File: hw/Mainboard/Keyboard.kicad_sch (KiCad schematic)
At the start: 5 parts, among them J2 KEYBOARD, U1 74LS145

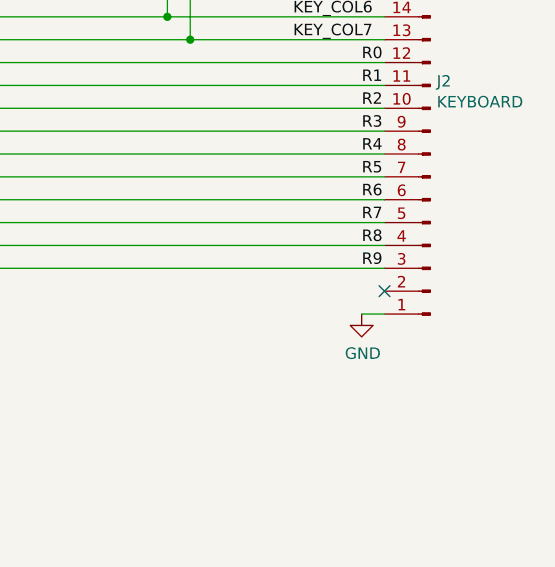
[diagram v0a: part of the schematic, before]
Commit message: hw: routed, but trace sizes need to be reviewed/fixed
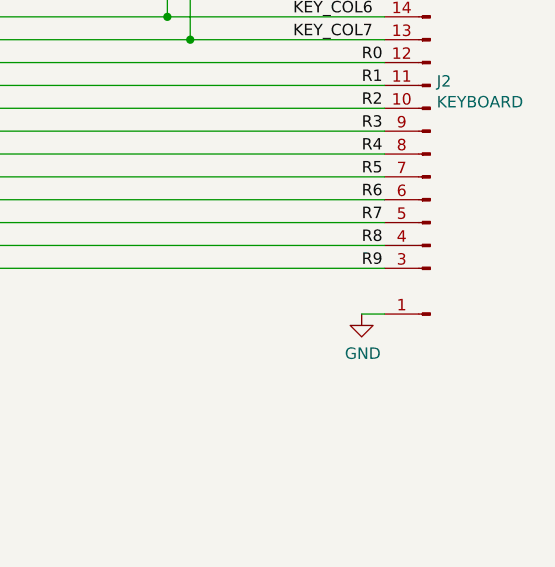
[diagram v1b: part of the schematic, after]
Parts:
- J2: footprint PET:Keyboard_Header_1x20_P2.54mm_Vertical -> Retrocomputing:CBM_PET_KEYBOARD_KEYED_20P; symbol Connector:Conn_01x20_Male -> Retrocomputing:CBM_PET_Keyboard_Conn_Keyed_20P
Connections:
- no-connect marks 1 -> 0
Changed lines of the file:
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@@
   (junction (at 190.5 87.63) (diameter 0) (color 0 0 0 0)
   )
-  (no_connect (at 214.63 118.11))
   (bus_entry (at 151.13 80.01) (size 2.54 2.54)
     (stroke (width 0) (type default) (color 0 0 0 0))
@@
     (pin "1")
   )
-  (symbol (lib_id "Connector:Conn_01x20_Male") (at 219.71 97.79 180) (unit 1)
+  (symbol (lib_id "Retrocomputing:CBM_PET_Keyboard_Conn_Keyed_20P") (at 219.71 97.79 180) (unit 1)
     (in_bom yes) (on_board yes)
     (property "Reference" "J2" (id 0) (at 220.4212 94.7928 0)
@@
       (effects (font (size 1.27 1.27)) (justify right))
     )
-    (property "Footprint" "PET:Keyboard_Header_1x20_P2.54mm_Vertical" (id 2) (at 219.71 97.79 0)
+    (property "Footprint" "Retrocomputing:CBM_PET_KEYBOARD_KEYED_20P" (id 2) (at 219.71 97.79 0)
       (effects (font (size 1.27 1.27)) hide)
     )
@@
     (pin "18")
     (pin "19")
-    (pin "2")
     (pin "20")
     (pin "3")

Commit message: hw: wip
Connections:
- net GND: no longer J2.1 (Pin_1)
- new net PD_GND: J2.1 (Pin_1)
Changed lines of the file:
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@@
+    (stroke (width 0) (type default) (color 0 0 0 0))
+  )
+  (wire (pts (xy 212.09 120.65) (xy 212.09 121.92))
     (stroke (width 0) (type default) (color 0 0 0 0))
   )
@@
     (pin "9")
   )
-  (symbol (lib_id "power:GND") (at 212.09 120.65 0) (unit 1)
-    (in_bom yes) (on_board yes)
-    (property "Reference" "#PWR07" (id 0) (at 212.09 127 0)
-      (effects (font (size 1.27 1.27)) hide)
-    )
-    (property "Value" "GND" (id 1) (at 212.217 125.0442 0))
-    (property "Footprint" "" (id 2) (at 212.09 120.65 0)
-      (effects (font (size 1.27 1.27)) hide)
-    )
-    (property "Datasheet" "" (id 3) (at 212.09 120.65 0)
-      (effects (font (size 1.27 1.27)) hide)
-    )
-    (pin "1")
-  )
   (symbol (lib_id "power:+5V") (at 180.34 57.15 0) (unit 1)
     (in_bom yes) (on_board yes)
@@
       (effects (font (size 1.27 1.27)) hide)
     )
+    (pin "1")
+  )
+  (symbol (lib_id "PET:PD_GND") (at 212.09 121.92 0) (unit 1)
+    (in_bom yes) (on_board yes) (fields_autoplaced)
+    (property "Reference" "#PWR0166" (id 0) (at 212.09 128.27 0)
+      (effects (font (size 1.27 1.27)) hide)
+    )
+    (property "Value" "PD_GND" (id 1) (at 212.09 127 0))
+    (property "Footprint" "" (id 2) (at 212.09 121.92 0)
+      (effects (font (size 1.27 1.27)) hide)
+    )
+    (property "Datasheet" "" (id 3) (at 212.09 121.92 0)
+      (effects (font (size 1.27 1.27)) hide)
+    )

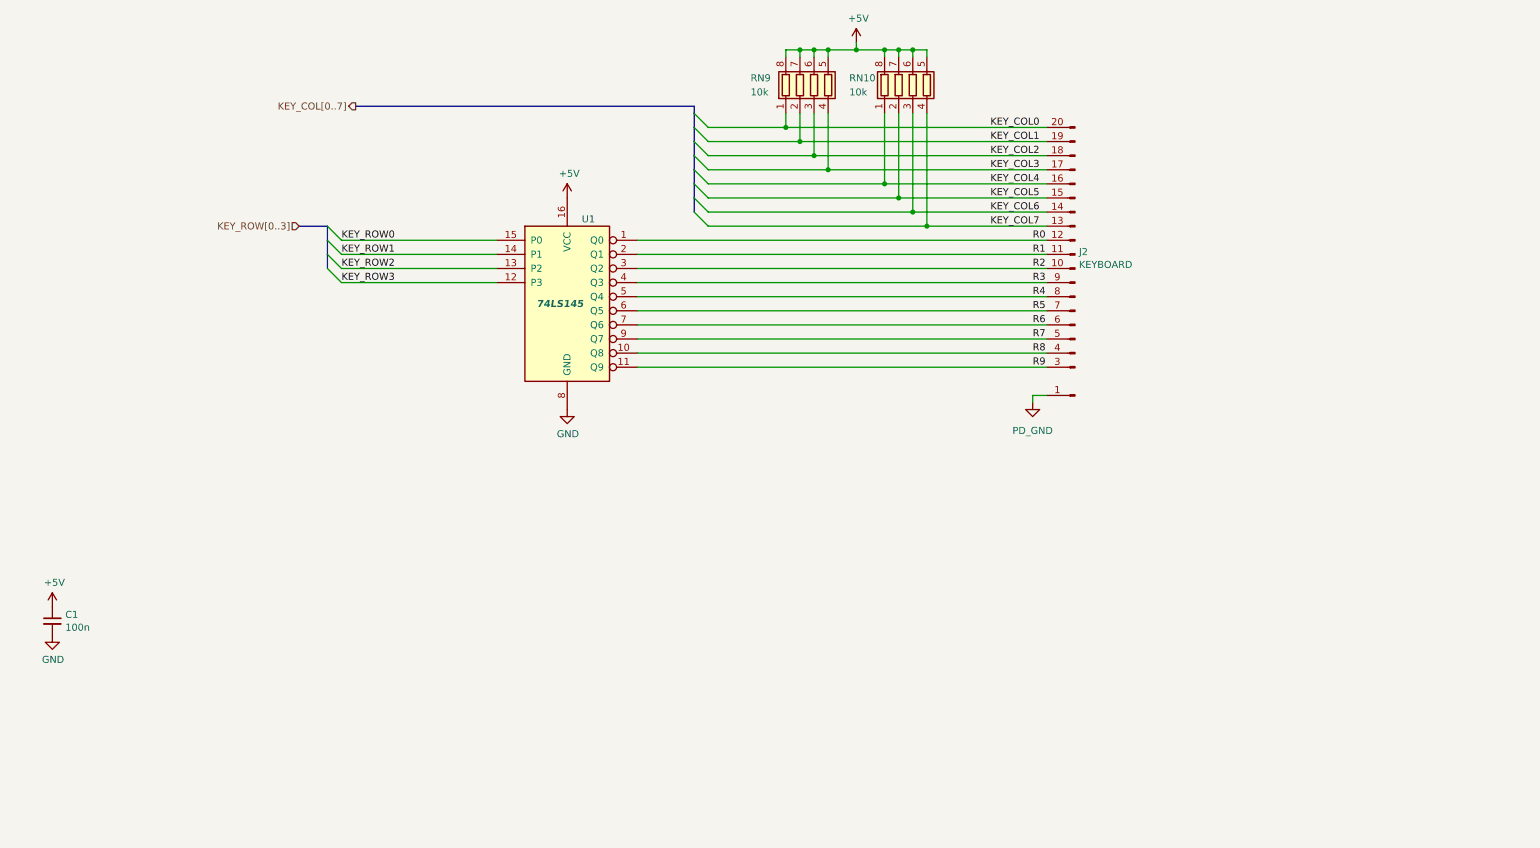
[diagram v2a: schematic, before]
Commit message: hw: larger schematic pages, routed w/netties
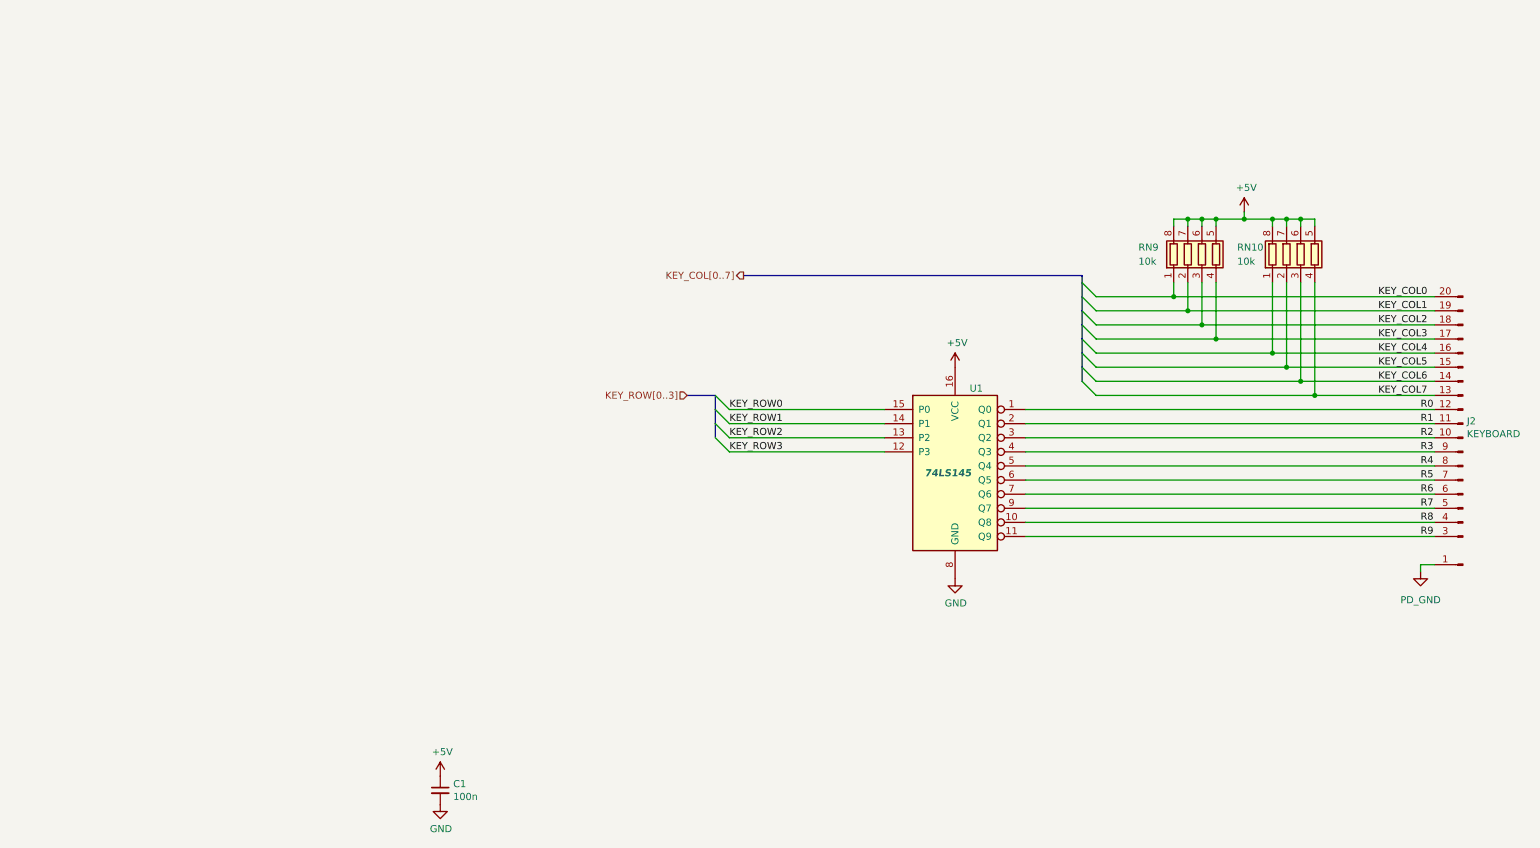
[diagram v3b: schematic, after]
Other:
- moved on the sheet: C1, J2, RN10, RN9, U1

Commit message: hw: wip
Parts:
- added NT35: +5V, PET:NetTie-2_SMD_Pad_1.6_to_0.4mm, symbol PET:PowerTie_2
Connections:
- net +5V: no longer names the net of C1.1, RN10.5 (R4.2), RN10.6 (R3.2), RN10.7 (R2.2), RN10.8 (R1.2), RN9.5 (R4.2), RN9.6 (R3.2), RN9.7 (R2.2), RN9.8 (R1.2), U1.16 (VCC)
- net +5V: now also NT35.2
- new net PD_5V: NT35.1
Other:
- moved on the sheet: C1

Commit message: jlcpcb - 1/19
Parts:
- J2: MOUSER 571-2-826646-0 -> (none)
- U1: MOUSER 595-SN74LS145DR -> (none)
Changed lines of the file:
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@@
       (effects (font (size 1.27 1.27)) hide)
     )
-    (property "MOUSER" "595-SN74LS145DR" (id 5) (at 198.12 133.35 0)
+    (property "MOUSER" "" (id 5) (at 198.12 133.35 0)
       (effects (font (size 1.27 1.27)) hide)
     )
@@
       (effects (font (size 1.27 1.27)) hide)
     )
-    (property "MOUSER" "571-2-826646-0" (id 4) (at 289.56 128.27 0)
+    (property "MOUSER" "" (id 4) (at 289.56 128.27 0)
       (effects (font (size 1.27 1.27)) hide)
     )
@@
       (effects (font (size 1.27 1.27)) hide)
     )
-    (property "Datasheet" "~" (id 3) (at 189.23 110.49 0)
+    (property "Datasheet" "https://datasheet.lcsc.com/lcsc/1810191219_Samsung-Electro-Mechanics-CL05B104KO5NNNC_C1525.pdf" (id 3) (at 189.23 110.49 0)
       (effects (font (size 1.27 1.27)) hide)
     )

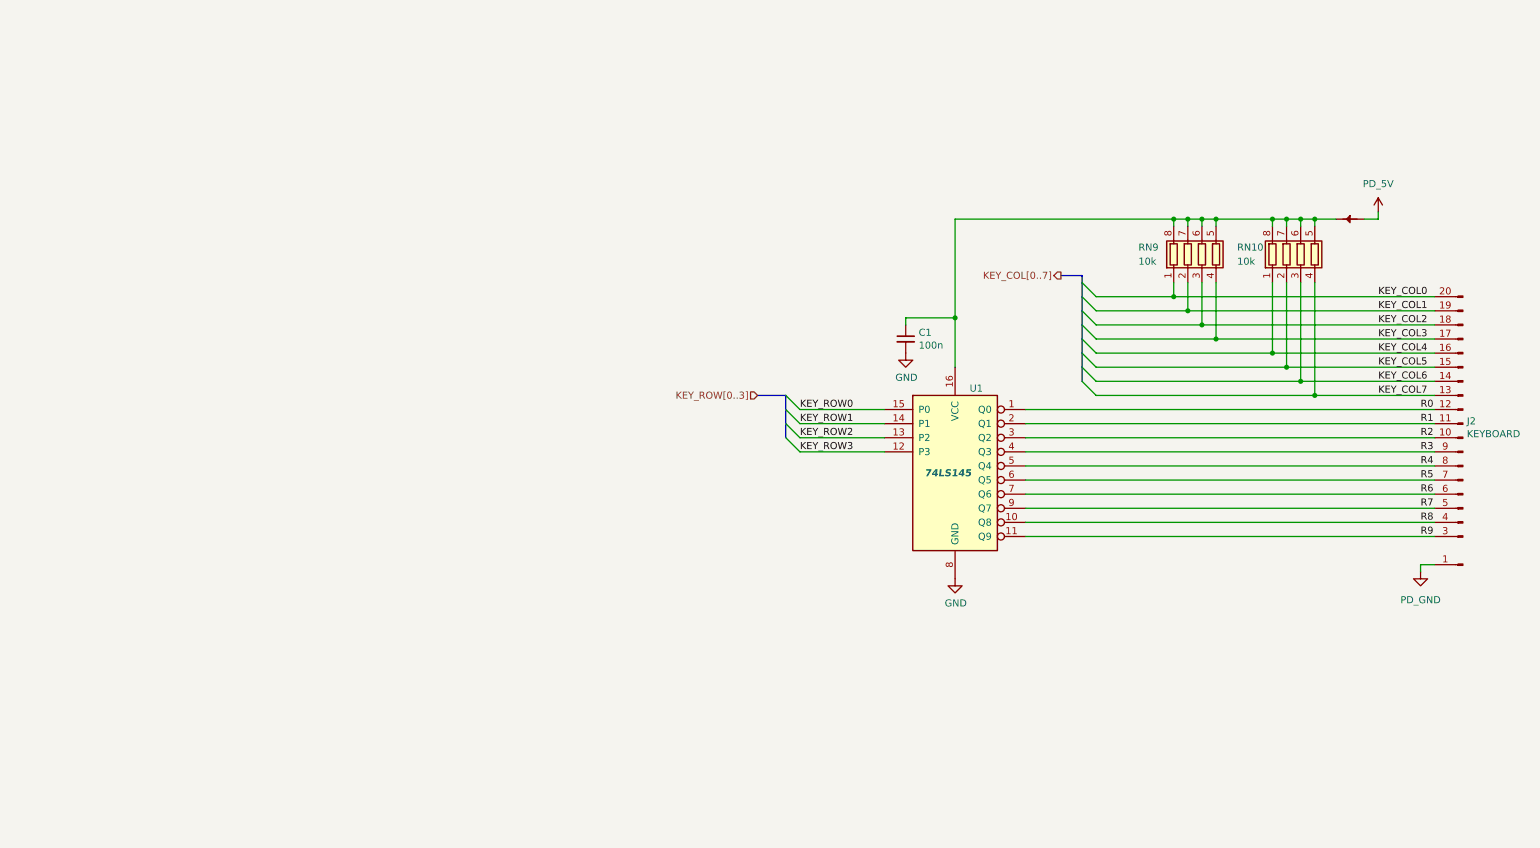
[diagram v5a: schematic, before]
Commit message: hw: tidy power and resize pages
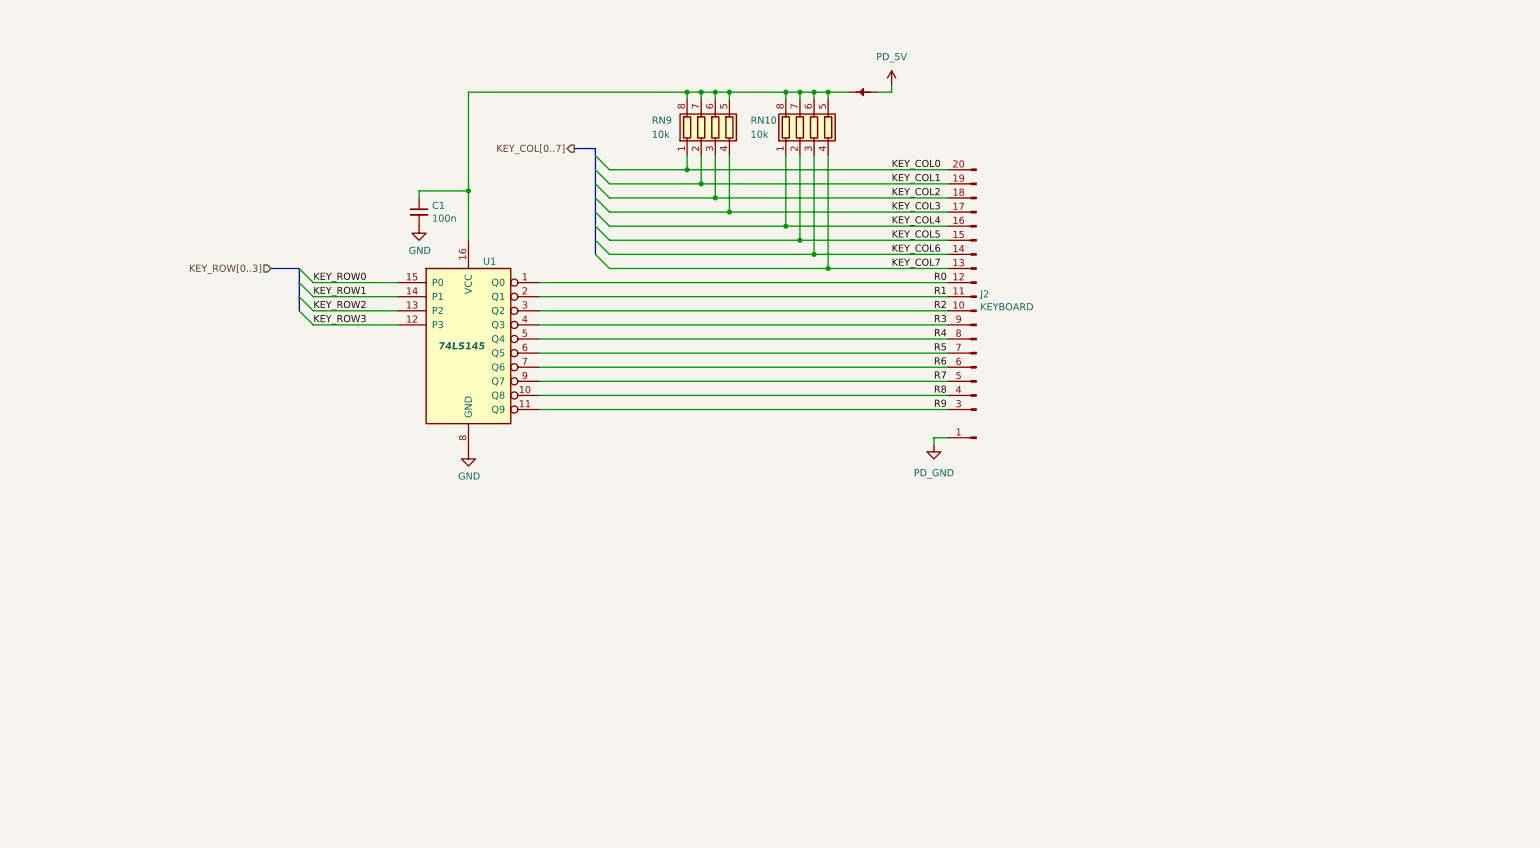
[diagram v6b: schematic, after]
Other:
- title: (none) -> CBM PET Mainboard Replacement
- moved on the sheet: C1, J2, RN10, RN9, U1
